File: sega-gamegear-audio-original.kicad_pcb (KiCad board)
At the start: 2 copper layers, 19 parts, among them CN1 CONN 2P, CN2 292161-6, IC1 TDA2822D, J1 PJ-307A

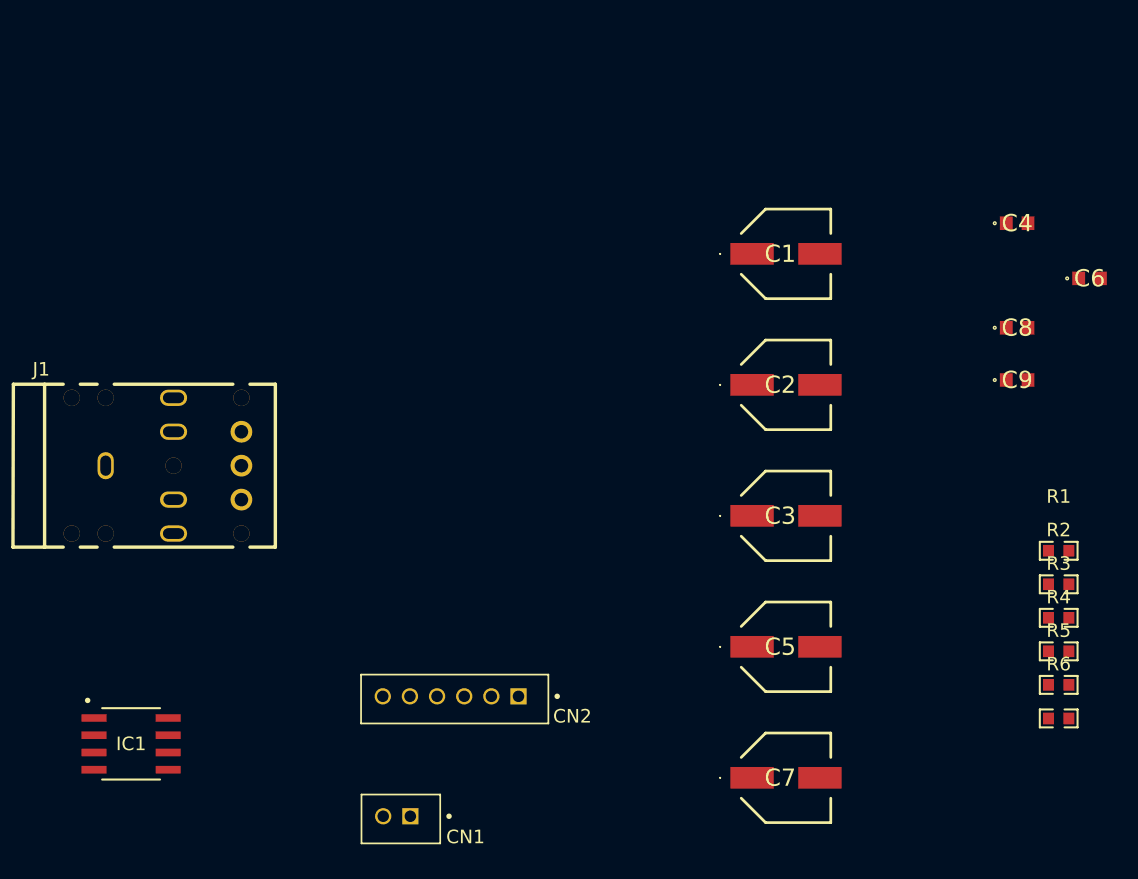
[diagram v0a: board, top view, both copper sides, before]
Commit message: update 3d models
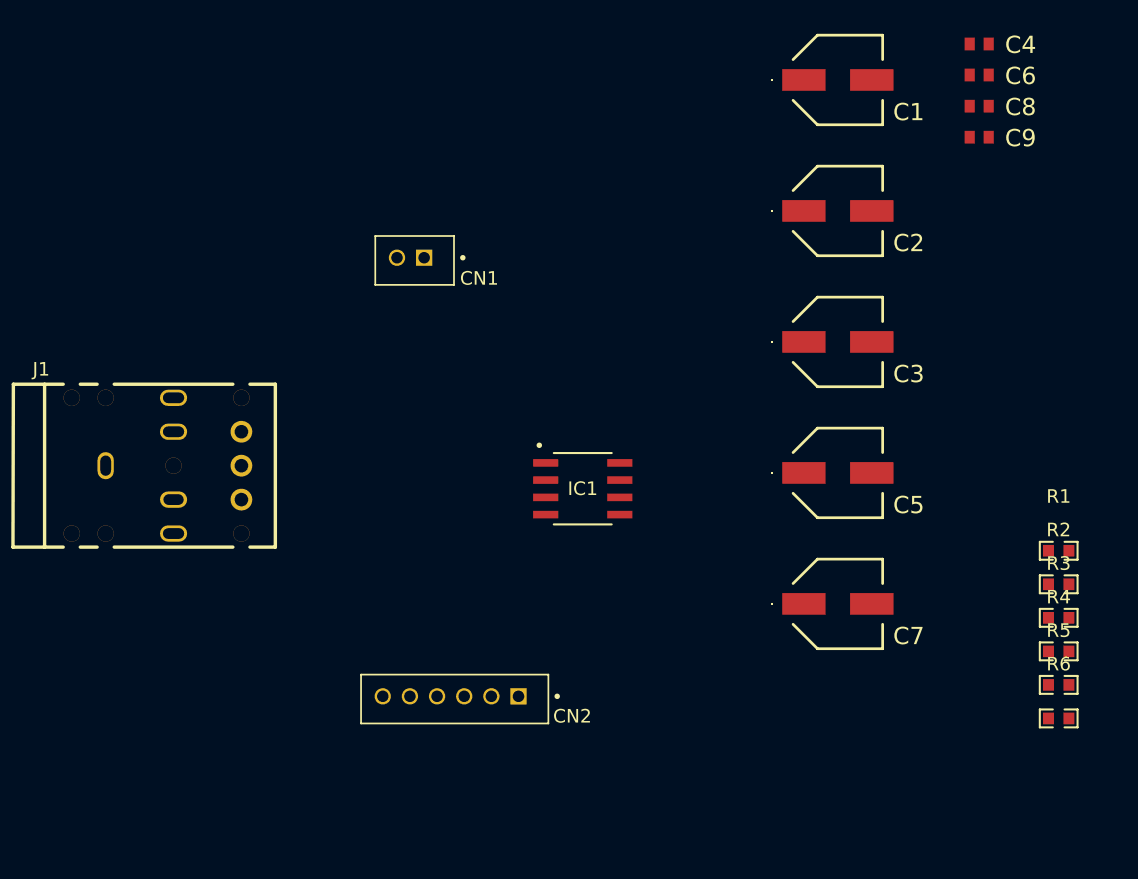
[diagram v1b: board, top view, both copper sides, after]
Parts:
- C1, C2: footprint Sega GameGear Audio Board Original:EEEFN1E101UP -> Sega GameGear Audio Board Original:C63D
- C3: footprint Sega GameGear Audio Board Original:EEEFT0J331AP -> Sega GameGear Audio Board Original:C63D
- C4, C6, C8, C9: footprint C0603C104K3RACTU:C0603 -> Sega GameGear Audio Board Original:C0603
- C5, C7: footprint Sega GameGear Audio Board Original:EEEFK1C470P -> Sega GameGear Audio Board Original:C63D
- moved CN1 41.2 mm to (179.3, 50.5)
- moved IC1 38.2 mm to (191.0, 67.6)
- moved C9 18.1 mm to (220.2, 41.7)
- moved C6 17.0 mm to (220.2, 37.1)
- moved C8 16.6 mm to (220.2, 39.4)
- moved C4 13.5 mm to (220.2, 34.8)
- moved C1 13.4 mm to (209.8, 37.5)
- moved C2 13.4 mm to (209.8, 47.1)
- moved C3 13.4 mm to (209.8, 56.8)
- moved C5 13.4 mm to (209.8, 66.4)
- moved C7 13.4 mm to (209.8, 76.0)

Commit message: fix courtyards
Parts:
- IC1: value TDA2822D -> Val**
- J1: value PJ-307A -> PJ-307
- moved C9 54.6 mm to (172.7, 68.6)
- moved C8 51.9 mm to (172.7, 60.4)
- moved C6 49.8 mm to (172.7, 52.3)
- moved C4 48.4 mm to (172.7, 44.1)
- moved R1 48.1 mm to (179.6, 59.7)
- moved R2 48.1 mm to (179.6, 62.1)
- moved R3 48.1 mm to (179.6, 64.6)
- moved R4 48.1 mm to (179.6, 67.1)
- moved R5 48.1 mm to (179.6, 69.5)
- moved R6 48.1 mm to (179.6, 72.0)
- moved C1 47.9 mm to (162.4, 44.9)
- moved C2 47.9 mm to (162.4, 54.5)
- moved C3 47.9 mm to (162.4, 64.2)
- moved C5 47.9 mm to (162.4, 73.8)
- moved C7 47.9 mm to (162.4, 83.5)
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
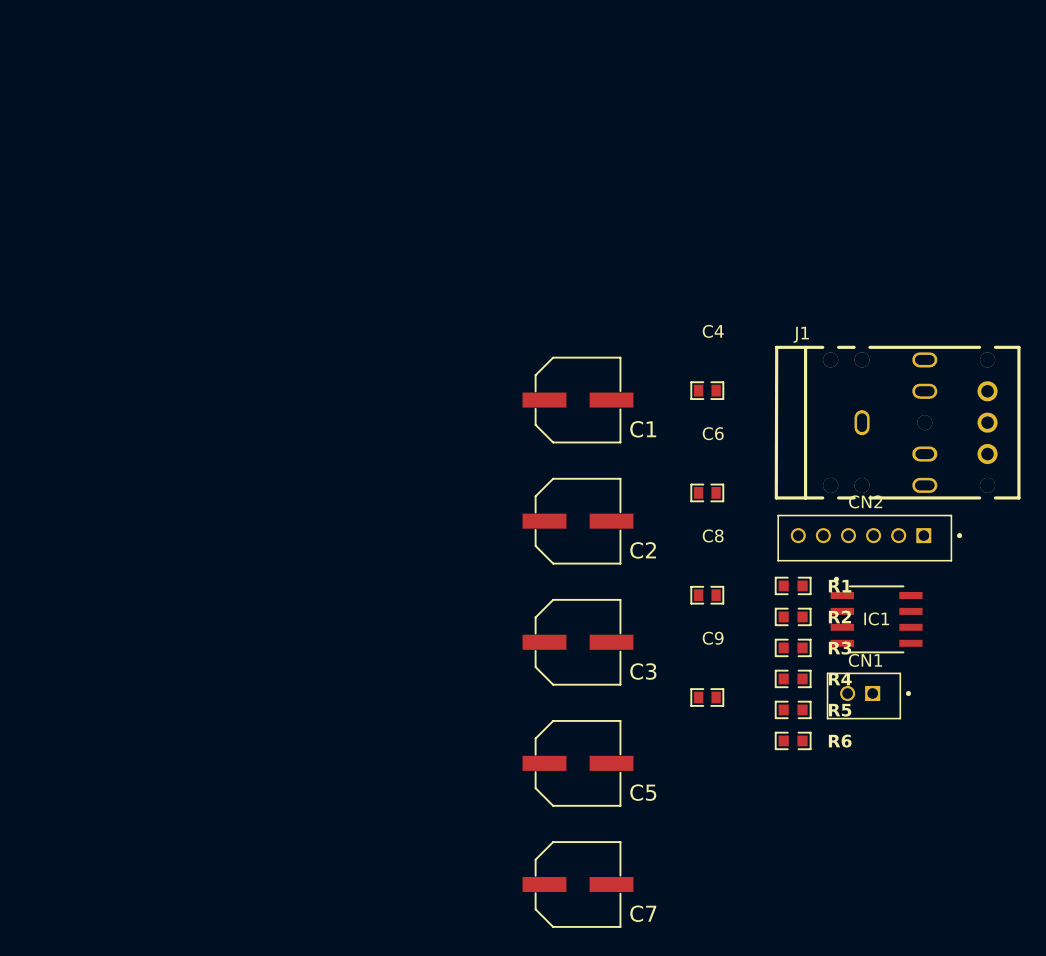
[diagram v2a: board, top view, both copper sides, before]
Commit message: fix solder mask
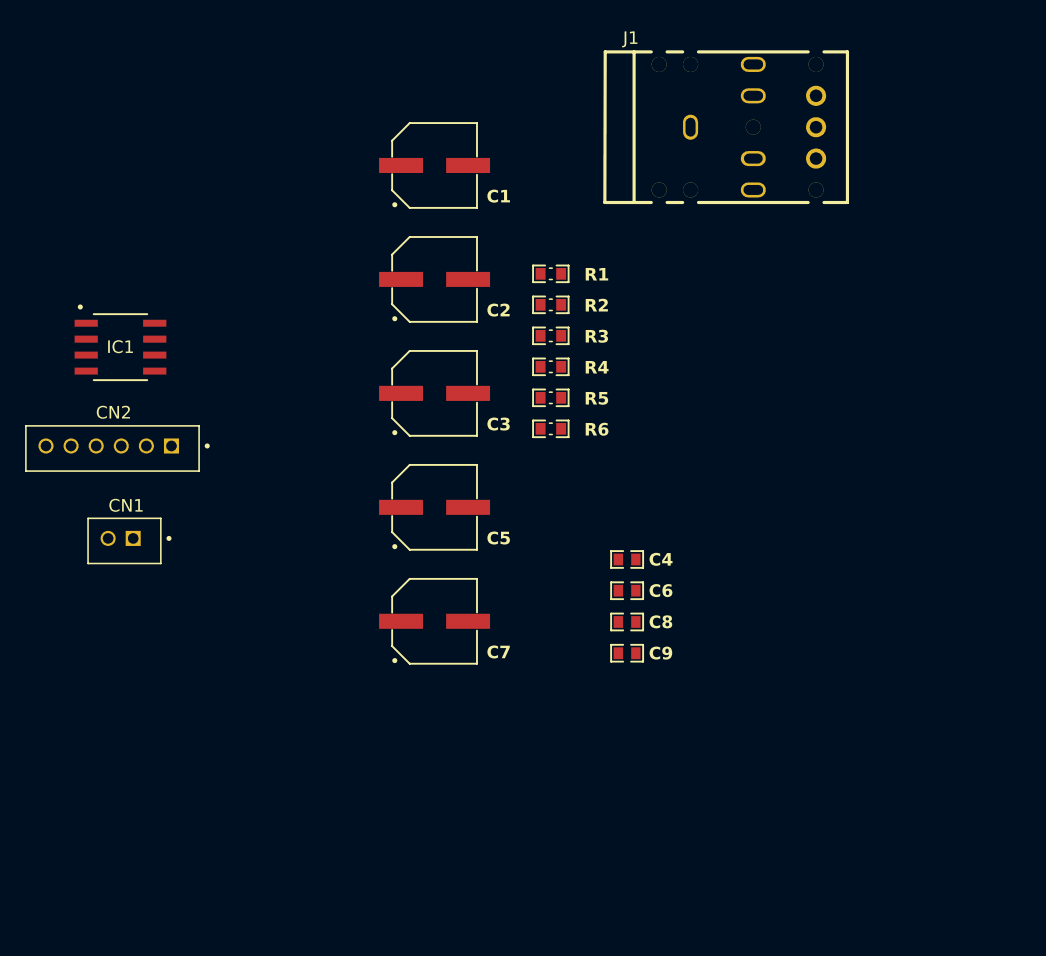
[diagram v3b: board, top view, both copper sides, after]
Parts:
- moved IC1 64.0 mm to (126.0, 40.6)
- moved CN2 60.4 mm to (130.0, 48.5)
- moved CN1 60.2 mm to (127.0, 55.9)
- moved R5 31.5 mm to (160.3, 44.7)
- moved R2 31.5 mm to (160.3, 37.3)
- moved R6 31.5 mm to (160.3, 47.1)
- moved R1 31.5 mm to (160.3, 34.8)
- moved R3 31.5 mm to (160.3, 39.7)
- moved R4 31.5 mm to (160.3, 42.2)
- moved J1 27.2 mm to (176.4, 23.1)
- moved C7 23.9 mm to (151.0, 62.5)
- moved C5 23.4 mm to (151.0, 53.4)
- moved C3 22.9 mm to (151.0, 44.3)
- moved C2 22.4 mm to (151.0, 35.2)
- moved C1 21.9 mm to (151.0, 26.2)
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
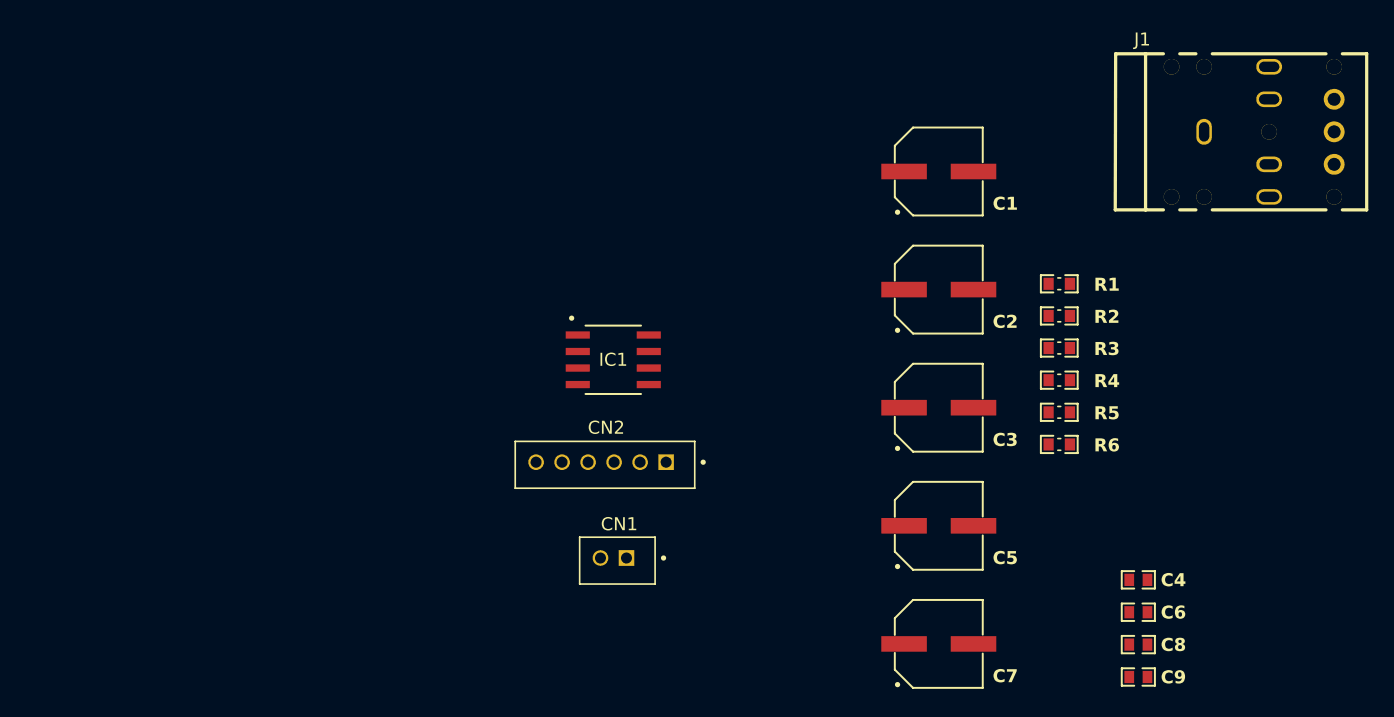
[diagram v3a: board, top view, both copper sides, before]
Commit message: fix pj307a footprint
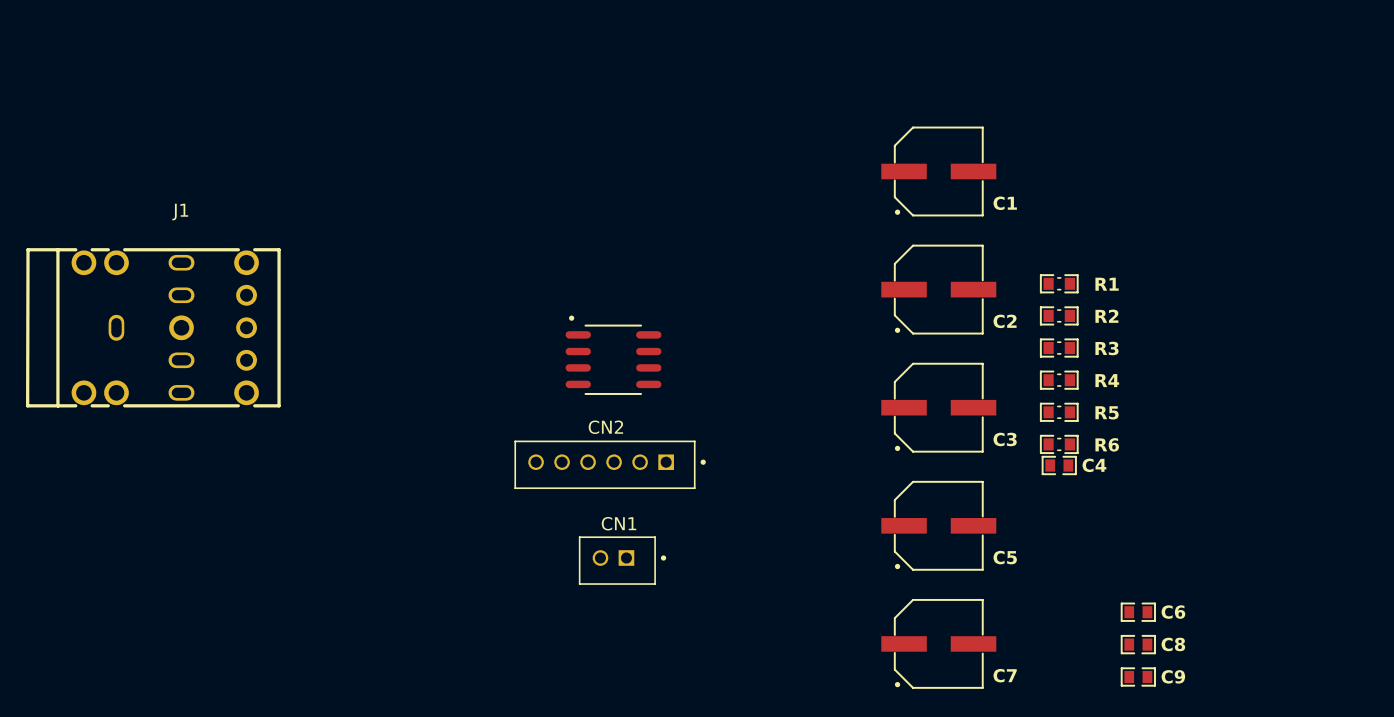
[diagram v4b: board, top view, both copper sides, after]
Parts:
- J1: value PJ-307 -> PJ-307A
- moved J1 85.0 mm to (92.8, 38.2)
- moved C4 10.7 mm to (160.3, 48.8)

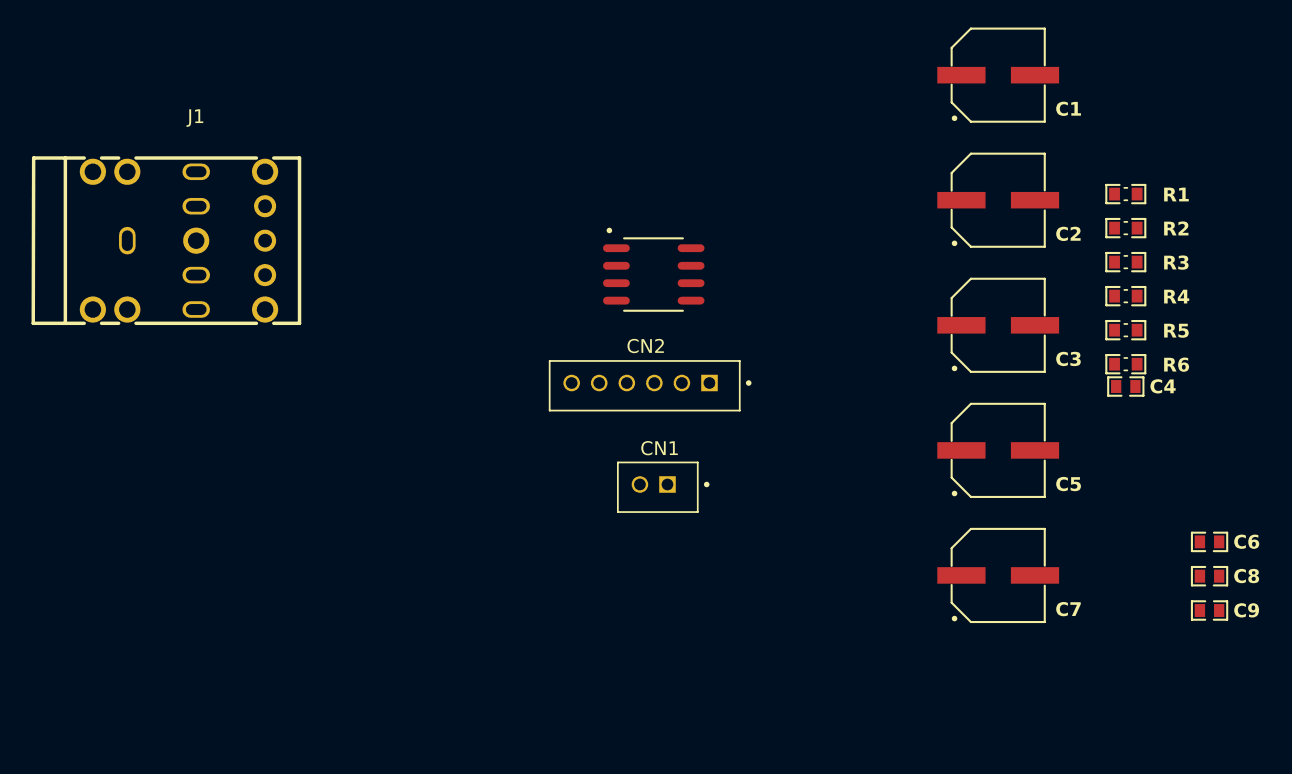
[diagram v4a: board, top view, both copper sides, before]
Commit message: add vr1 footprint
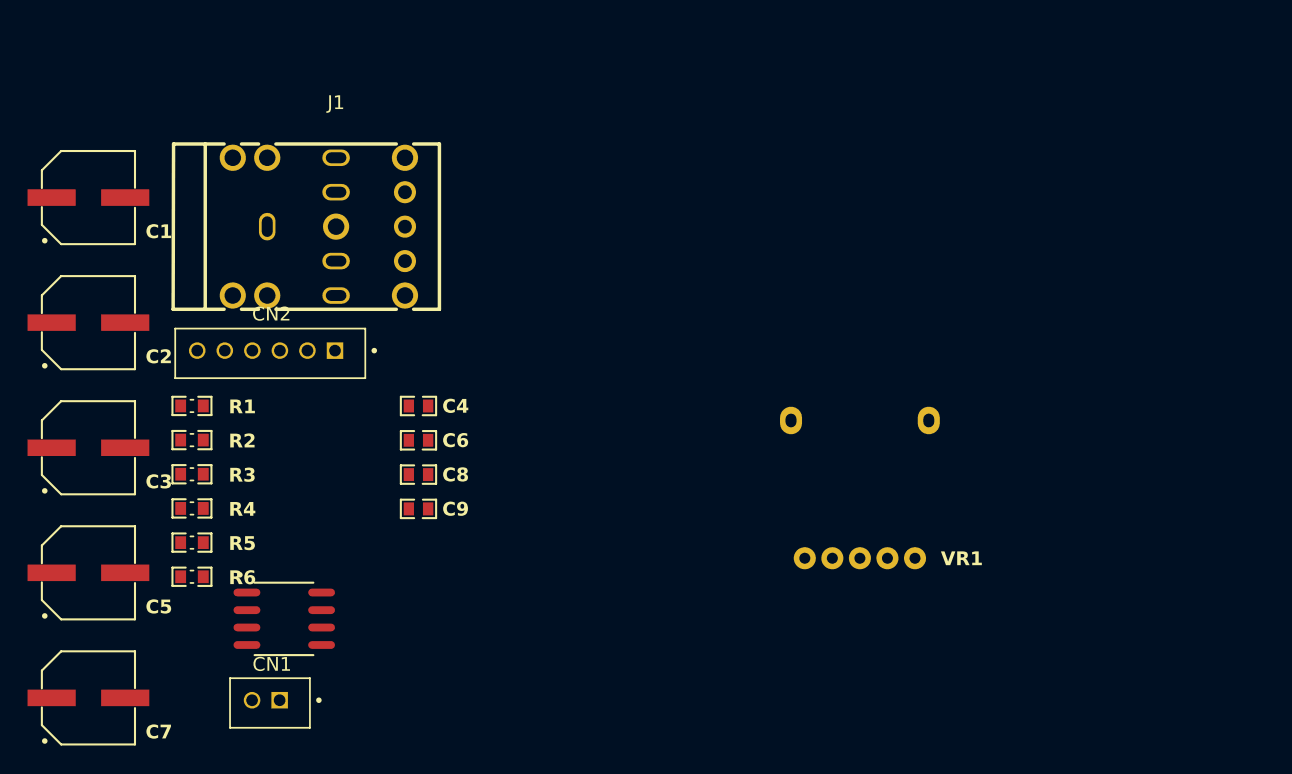
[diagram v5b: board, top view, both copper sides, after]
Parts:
- added VR1: EVUTV2B19A14, Sega GameGear Audio Board Original:EVUTV2B19A14, F.Cu at (141.0, 51.2)
- IC1: value Val** -> TDA2822D
- moved R6 69.5 mm to (92.5, 62.6)
- moved R5 69.5 mm to (92.5, 60.1)
- moved R4 69.5 mm to (92.5, 57.6)
- moved R3 69.5 mm to (92.5, 55.1)
- moved R2 69.5 mm to (92.5, 52.7)
- moved R1 69.5 mm to (92.5, 50.2)
- moved C1 66.6 mm to (85.0, 35.1)
- moved C2 66.6 mm to (85.0, 44.1)
- moved C3 66.6 mm to (85.0, 53.2)
- moved C5 66.6 mm to (85.0, 62.3)
- moved C7 66.6 mm to (85.0, 71.4)
- moved C6 57.9 mm to (108.9, 52.7)
- moved C8 57.9 mm to (108.9, 55.2)
- moved C9 57.9 mm to (108.9, 57.7)
- moved C4 51.4 mm to (108.9, 50.2)
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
